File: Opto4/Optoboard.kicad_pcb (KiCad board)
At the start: 2 copper layers, 64.6 x 33.8 mm, 39 parts, among them J1 S1 Connector, J2 S2 Connector, J3 S3 Connector, J4 S4 Connector, J5 Conn_01x06, U1 6N135, U2 6N135, U3 6N135, U4 6N135, U5 L7805

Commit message: Added files
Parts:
- removed the REF** at (176.1, 110.1)
- removed the REF** at (166.7, 94.9)
- removed the REF** at (225.1, 94.1)
- added P1: CONN_01X02, Pin_Headers:Pin_Header_Straight_1x02, F.Cu at (213.8, 94.3)
- added REF**: 1pin, Connect:1pin, F.Cu at (224.6, 94.8)
- added REF**: 1pin, Connect:1pin, F.Cu at (166.9, 95.0)
- added REF**: 1pin, Connect:1pin, F.Cu at (176.5, 111.3)
- moved 12V_IN 1.86 mm to (167.8, 116.6)
- moved C1 1.83 mm to (177.0, 119.8)
- moved D1 1.39 mm to (167.8, 122.8)
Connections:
- J5 pad 1: +5V -> Net-(J5-Pad1)
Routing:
- net +12V: track 101.0 -> 106.3 mm
- net +5V: track 131.8 -> 137.0 mm
- net GND: track 70.2 -> 74.9 mm
- net Net-(J5-Pad1): track 0.00 -> 4.57 mm
- net S1: track 24.1 -> 20.3 mm
- net Net-(12V_IN1-Pad1): track 7.71 -> 7.03 mm
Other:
- outline, holes or cut-outs redrawn
- board text added: "EN 5V"

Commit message: Modified to 3.3V and 5V compatibility
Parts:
- removed 12V_IN: Screw_Terminal_01x02, Connectors_Terminal_Blocks:TerminalBlock_4UCON_19963_02x3.5mm_Straight
- removed the REF** at (224.6, 94.8)
- removed the REF** at (166.9, 95.0)
- removed the REF** at (176.5, 111.3)
- added 12V_IN1: Screw_Terminal_01x02, Connectors_Terminal_Blocks:TerminalBlock_Pheonix_MKDS1.5-2pol, F.Cu at (169.0, 116.2)
- added G***: LOGO, Hardware:EP_Logo, B.Cu at (175.3, 102.7)
- added REF**: 1pin, Connectors:1pin, F.Cu at (224.6, 94.8)
- added REF**: 1pin, Connectors:1pin, F.Cu at (167.2, 95.1)
- U5: value L7805 -> LM2937ET-3.3; footprint TO_SOT_Packages_SMD:TO-252-2Lead -> TO_SOT_Packages_SMD:SOT-223
- moved U5 1.39 mm to (174.5, 103.2), turned to 180 degrees
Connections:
- net +5V renamed +3V3
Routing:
- net GND: track 74.9 -> 98.4 mm, vias 2 -> 3
- net +12V: track 106.3 -> 101.5 mm
- net Net-(12V_IN1-Pad1): track 7.03 -> 9.08 mm
- net +3V3: track 137.0 -> 136.1 mm
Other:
- board text added: "3V3"
- board text added: "EN 3V3"
- board text added: "Opto-isolator board Rev: 1.1 - Opto version: 4"
- board text removed: "5V"
- board text removed: "EN 5V"
- board text removed: "Opto-isolator board Rev: 1.0 - Opto version: 4"

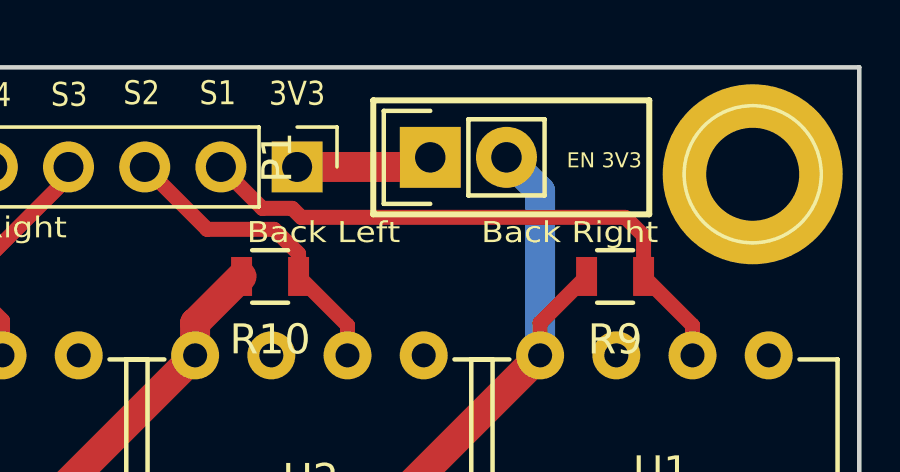
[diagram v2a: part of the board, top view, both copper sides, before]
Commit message: Added pdf and images
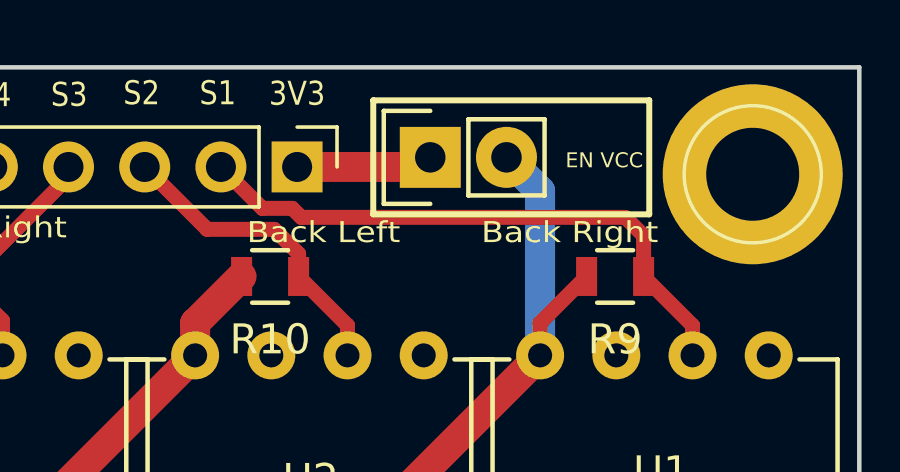
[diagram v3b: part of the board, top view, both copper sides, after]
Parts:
- removed the G*** at (175.3, 102.7)
- added G***: LOGO, Hardware:EP_Logo_3, B.Cu at (173.5, 102.4)
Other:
- board text added: "EN VCC"
- board text removed: "EN 3V3"

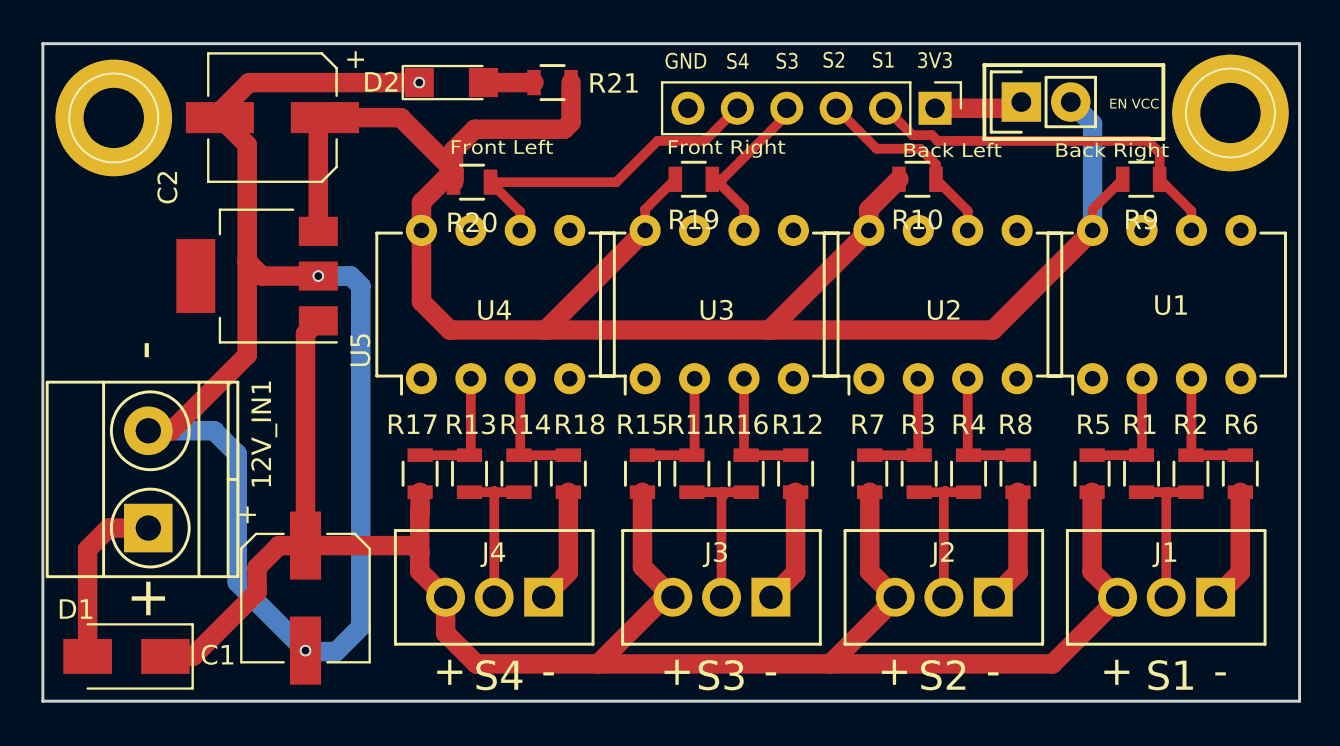
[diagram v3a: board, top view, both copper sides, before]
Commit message: Updated the regulator and some small modifs
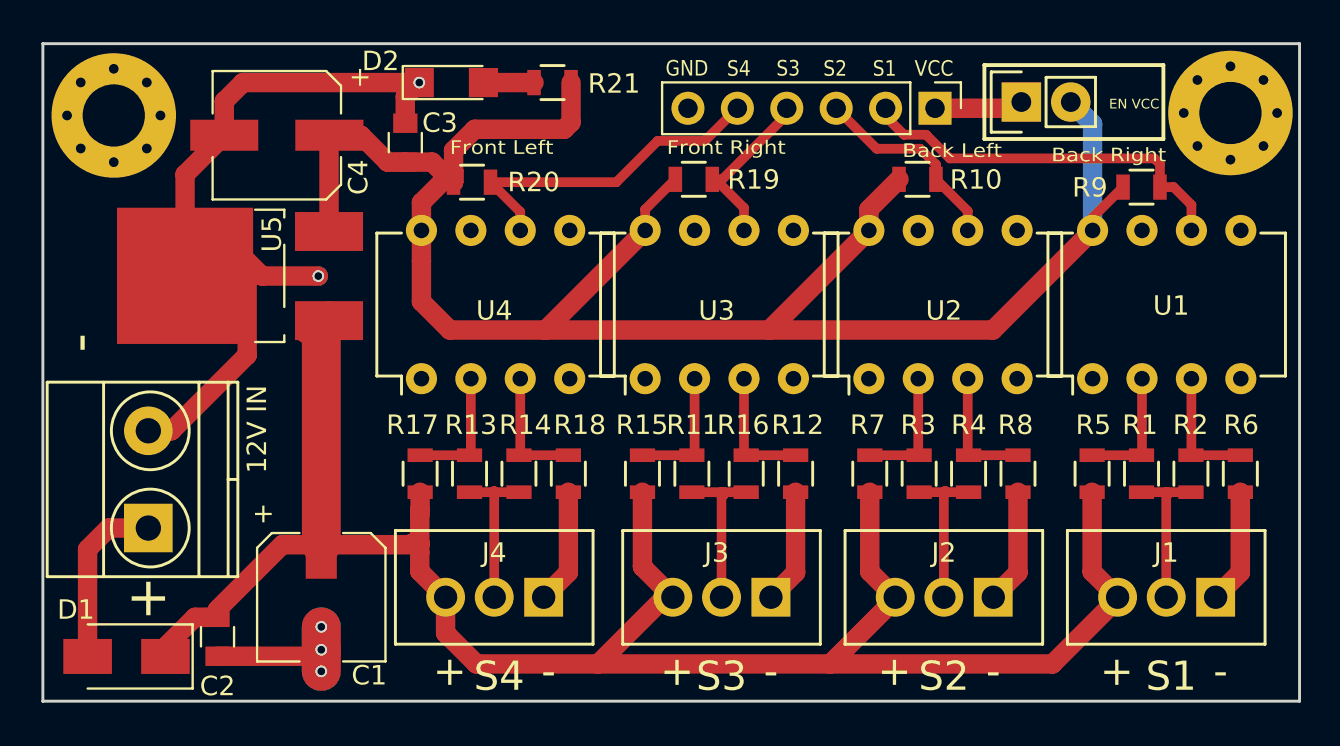
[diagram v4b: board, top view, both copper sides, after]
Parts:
- removed REF** (x2): 1pin, Connectors:1pin
- added C3: 100n, Capacitors_SMD:C_0805, F.Cu at (182.2, 96.4)
- added C4: 100u, Capacitors_SMD:CP_Elec_6.3x5.3, F.Cu at (175.6, 96.0)
- added MK1: Mounting_Hole, Mounting_Holes:MountingHole_3.2mm_M3_Pad_Via, F.Cu at (224.6, 94.8)
- added MK2: Mounting_Hole, Mounting_Holes:MountingHole_3.2mm_M3_Pad_Via, F.Cu at (167.2, 95.0)
- 12V IN: renamed from 12V_IN1
- C1: value 470u -> 100u
- C2: value 470uF -> 100n; footprint Capacitors_SMD:CP_Elec_6.3x5.3 -> Capacitors_SMD:C_0805
- R21: value R -> 1K
- U5: value LM2937ET-3.3 -> LM7805; footprint TO_SOT_Packages_SMD:SOT-223 -> TO_SOT_Packages_SMD:TO-252-2Lead
- moved C2 26.8 mm to (172.5, 121.8), turned to 270 degrees
- moved G*** 1.05 mm to (174.5, 102.5)
- moved C1 0.81 mm to (177.9, 119.7)
- moved R9 0.40 mm to (220.0, 98.7)
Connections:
- C2 pad 1: +3V3 -> +12V
- P1 pad 2: +3V3 -> VCC
- R10 pad 2: +3V3 -> VCC
- R19 pad 2: +3V3 -> VCC
- R20 pad 2: +3V3 -> VCC
- R21 pad 1: +3V3 -> VCC
- R9 pad 2: +3V3 -> VCC
- U1 pad 8: +3V3 -> VCC
- U2 pad 8: +3V3 -> VCC
- U3 pad 8: +3V3 -> VCC
- U4 pad 8: +3V3 -> VCC
- U5 pad 3: +3V3 -> VCC
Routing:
- net +3V3: track 136.1 -> 0.00 mm
- net VCC: track 0.00 -> 134.3 mm
- net GND: track 98.4 -> 72.0 mm, vias 3 -> 5
- net +12V: track 101.5 -> 102.6 mm
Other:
- board text added: "Opto-isolator board Rev: 1.2 - Opto version: 4"
- board text added: "VCC"
- board text removed: "3V3"
- board text removed: "Opto-isolator board Rev: 1.1 - Opto version: 4"
